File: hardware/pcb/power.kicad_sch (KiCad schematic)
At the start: 74 parts, among them J1 XT30PW-F, J12 Solar, J13 USB-C, Q3 AO3407, Q4 BSS123, Q5 AO3407, U1 AP63203WU, U11 USBLC6, U12 IP2326, U7 CN3722, U8 MT3608B

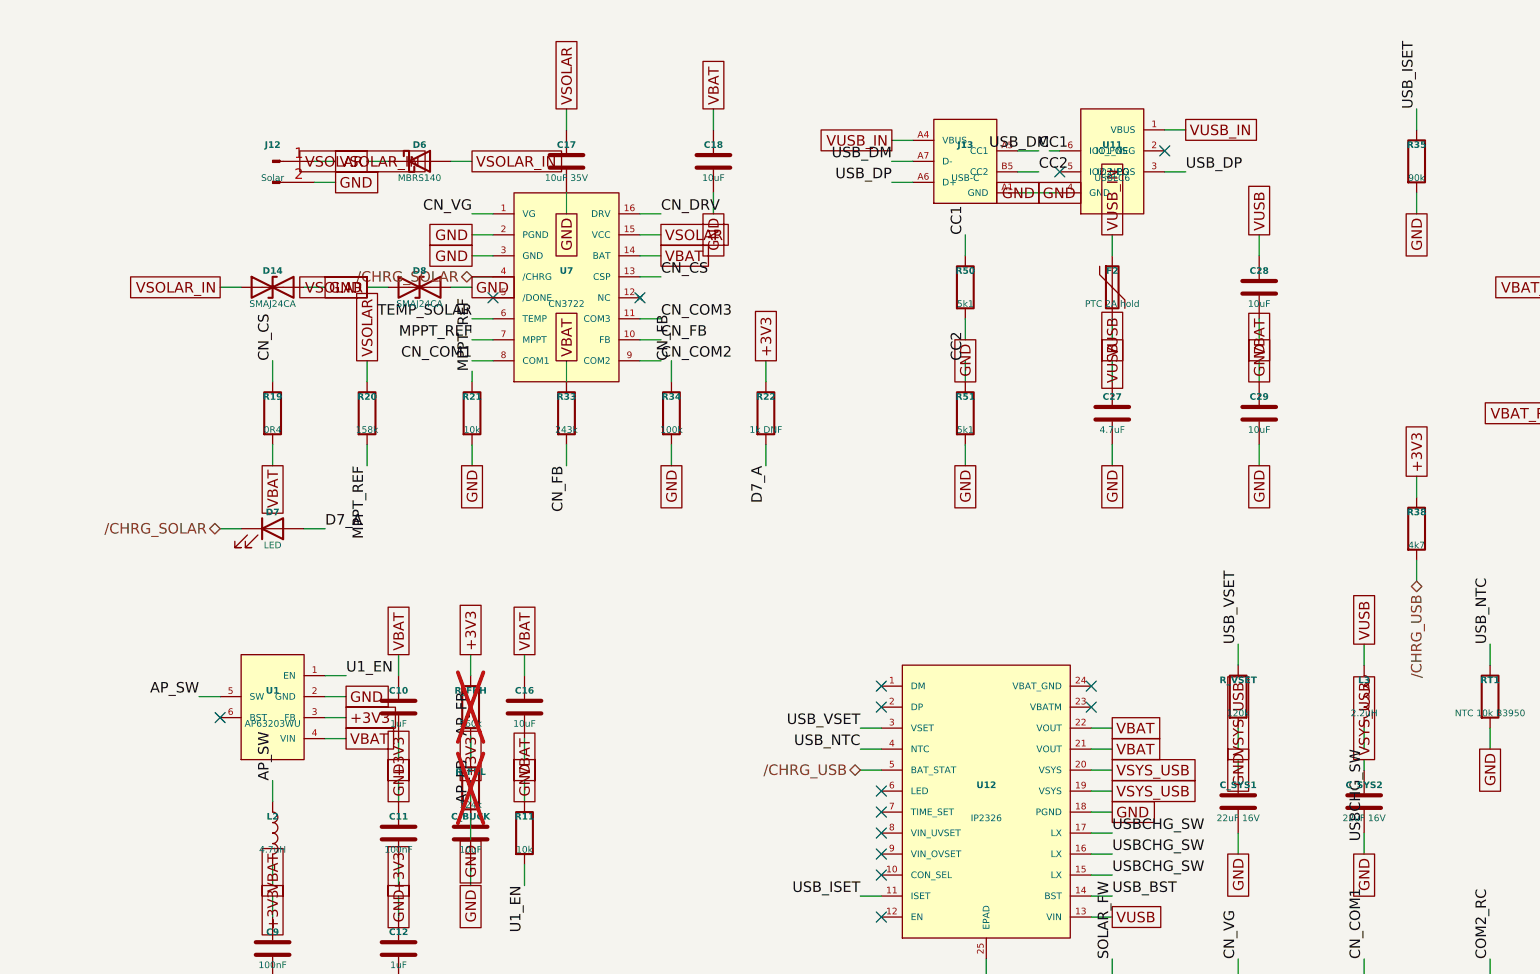
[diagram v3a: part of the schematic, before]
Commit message: hw(pcb): apply blocker #9 — AP63203 renumber + BST cap, ESD symbol fixes, value syncs
All eight required edits from the 2026-07-14 component verification,
applied by pin-name-preserving renumber (positions untouched, so the
stub+label wiring stays electrically identical; only footprint pad
mapping changes):

- U1: lib symbol renamed welld:AP63203WU, pins renumbered to the
  verified Diodes map (FB=1, EN=2, VIN=3, GND=4, SW=5, BST=6),
  footprint TSOT-23-6. NEW C_BST_AP 100 nF placed and wired on new net
  AP_BST (BST <-> SW) — the bootstrap cap without which the 3.3 V rail
  cannot start. BST no_connect removed.
- U11 USBLC6 renumbered to the ST map (I/O1=1, GND=2, I/O2=3, I/O2'=4,
  VBUS=5, I/O1'=6).
- D1/D12 PRTR5V0U2X redrawn as the real 4-pin SOT-143B (GND=1, I/O1=2,
  I/O2=3, VCC=4); phantom VCC2/GND2 pins, their 4 stubs and 4 labels
  removed; instance pin uuids pruned.
- D9/D10 -> SMAJ5.0A; U12 footprint -> QFN-24-1EP_4x4mm_P0.5mm;
  FB1 -> 0603; C28/C29/C_SYS1/C_SYS2 -> 25 V ratings.
- Intent tables in kicad_wire_script.py remapped placeholder-safe;
  netlist_check.py re-run: 393 pins, 78 nets (+AP_BST), 20 no-connects,
  ZERO mismatches. All five sheets pass the balance check.

Co-Authored-By: Claude Fable 5 <noreply@anthropic.com>
Claude-Session: https://claude.ai/code/session_01VtMFY5Q94iYbsNPpLcPJyK
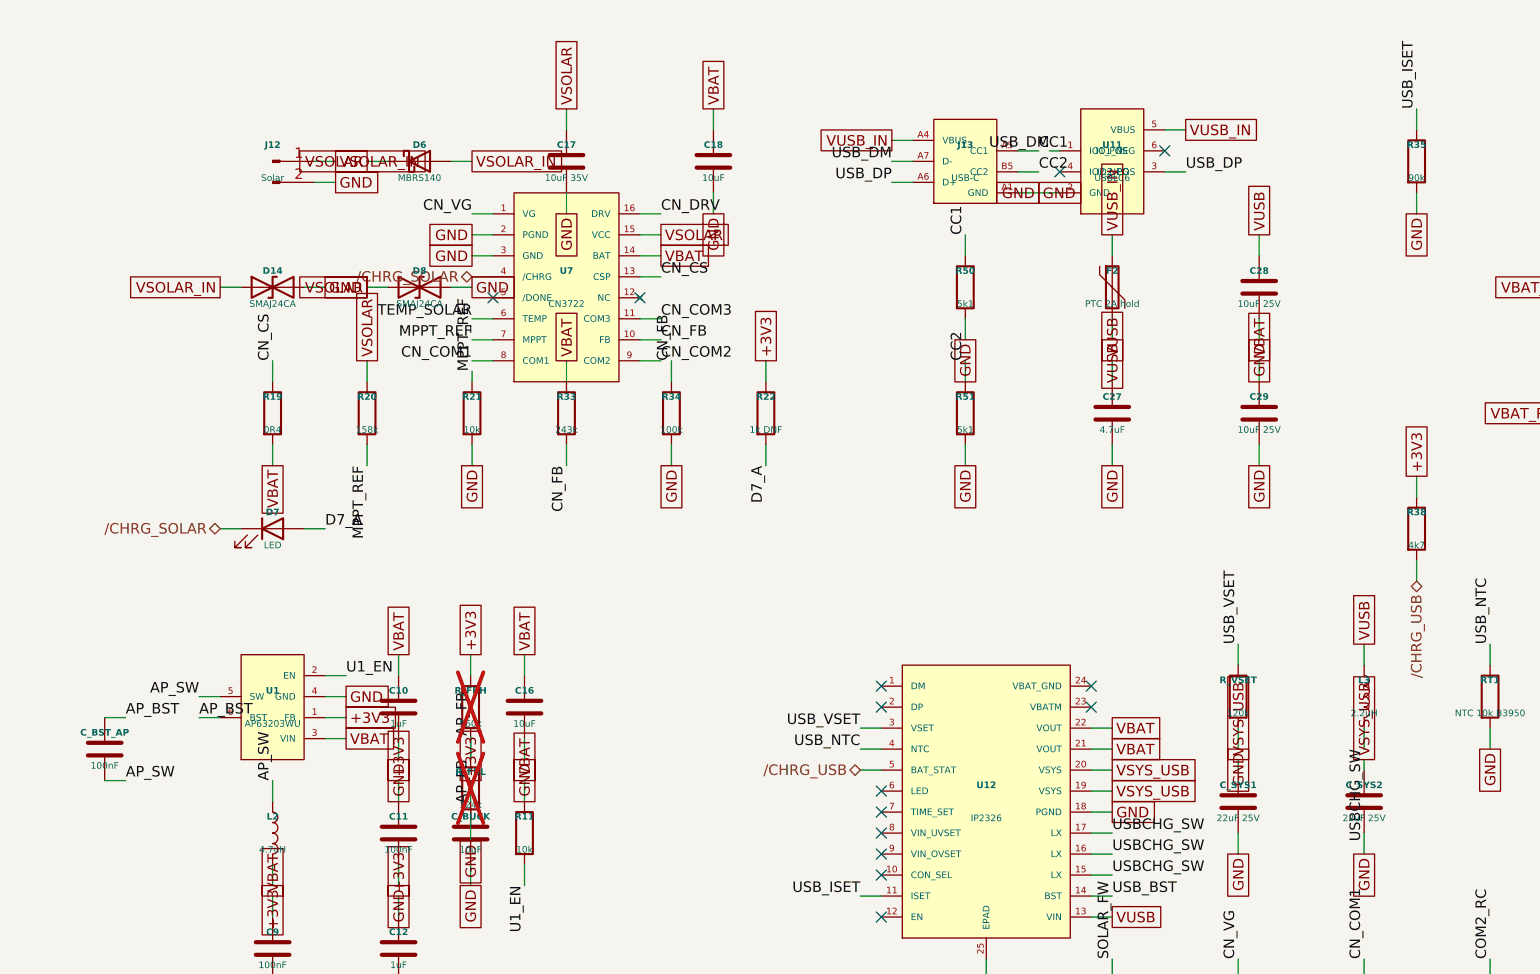
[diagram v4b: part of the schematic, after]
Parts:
- added C_BST_AP: 100nF, Capacitor_SMD:C_0402_1005Metric, symbol Device:C
- C28, C29: value 10uF -> 10uF 25V
- C_SYS1, C_SYS2: value 22uF 16V -> 22uF 25V
- U1: footprint Package_TO_SOT_SMD:SOT-23-6 -> Package_TO_SOT_SMD:TSOT-23-6; symbol welld:AP63205WU -> welld:AP63203WU
- U12: footprint welld:IP2326_TBD -> Package_DFN_QFN:QFN-24-1EP_4x4mm_P0.5mm_EP2.6x2.6mm
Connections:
- net +3V3: now also U1.1 (FB); no longer U1.3 (FB)
- net AP_SW: now also C_BST_AP.2
- net GND: now also U1.4 (GND), U11.2 (GND); no longer U1.2 (GND), U11.4 (GND)
- net U1_EN: now also U1.2 (EN); no longer U1.1 (EN)
- net USB_DM: now also U11.1 (IO1_POS); no longer U11.6 (IO1_POS)
- net VBAT: now also U1.3 (VIN); no longer U1.4 (VIN)
- net VUSB_IN: now also U11.5 (VBUS); no longer U11.1 (VBUS)
- net AP_BST: now reaches U1.6 (BST)
- net AP_BST: now also C_BST_AP.1
- no-connect marks 15 -> 14
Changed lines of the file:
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@@
 			)
 		)
-		(property "Value" "10uF"
+		(property "Value" "10uF 25V"
 			(at 185.42 41.37 0)
 			(show_name no)
@@
 	)
 	(symbol
-		(lib_id "welld:AP63205WU")
+		(lib_id "welld:AP63203WU")
 		(at 66.04 90.17 0)
 		(unit 1)
@@
 			)
 		)
-		(property "Footprint" "Package_TO_SOT_SMD:SOT-23-6"
+		(property "Footprint" "Package_TO_SOT_SMD:TSOT-23-6"
 			(at 0 0 0)
 			(hide yes)
@@
 			)
 		)
-		(property "Value" "10uF"
+		(property "Value" "10uF 25V"
 			(at 185.42 56.61 0)
 			(show_name no)
@@
 	(symbol
 		(lib_id "Device:C")
+		(at 45.72 95.25 0)
+		(unit 1)
+		(body_style 1)
+		(exclude_from_sim no)
+		(in_bom yes)
+		(on_board yes)
+		(in_pos_files yes)
+		(dnp no)
+		(fields_autoplaced yes)
+		(property "Reference" "C_BST_AP"
+			(at 45.72 93.25 0)
+			(show_name no)
+			(do_not_autoplace no)
+			(effects
+				(font
+					(size 0.8 0.8)
+					(bold yes)
+				)
+			)
+		)
+		(property "Value" "100nF"
+			(at 45.72 97.25 0)
+			(show_name no)
+			(do_not_autoplace no)
+			(effects
+				(font
+					(size 0.8 0.8)
+				)
+			)
+		)
+		(property "Footprint" "Capacitor_SMD:C_0402_1005Metric"
+			(at 0 0 0)
+			(hide yes)
+			(show_name no)
+			(do_not_autoplace no)
+			(effects
+				(font
+					(size 0.8 0.8)
+				)
+			)
+		)
+		(property "Datasheet" ""
+			(at 0 0 0)
+			(hide yes)
+			(show_name no)
+			(do_not_autoplace no)
+			(effects
+				(font
+					(size 0.8 0.8)
+				)
+			)
+		)
+		(property "Description" "100nF 0402 MT3608B bootstrap cap BST(pin6)->SW mandatory gate driver supply"
+			(at 0 0 0)
+			(hide yes)
+			(show_name no)
+			(do_not_autoplace no)
+			(effects
+				(font
+					(size 0.8 0.8)
+				)
+			)
+		)
+		(property "LCSC" "C14663"
+			(at 0 0 0)
+			(hide yes)
+			(show_name no)
+			(do_not_autoplace no)
+			(effects
+				(font
+					(size 0.8 0.8)
+				)
+			)
+		)
+		(pin "1"
+		)
+		(pin "2"
+		)
+		(instances
+			(project "welld"
+				(path "/58c9365f-ec30-52a7-98fc-0e15b15bee29"
+					(reference "C_BST_AP")
+					(unit 1)
+				)
+				(path "/58c9365f-ec30-52a7-98fc-0e15b15bee29/64fba67a-e021-5c3c-b6fb-14c5c55ee35f/aaaa0003-b000-4000-8000-000000000001"
+					(reference "C_BST_AP")
+					(unit 1)
+				)
+			)
+		)
+	)
+	(symbol
+		(lib_id "Device:C")
 		(at 90 105.41 0)
 		(unit 1)
@@
 			)
 		)
-		(property "Footprint" "welld:IP2326_TBD"
+		(property "Footprint" "Package_DFN_QFN:QFN-24-1EP_4x4mm_P0.5mm_EP2.6x2.6mm"
 			(at 0 0 0)
 			(hide yes)
@@
 			)
 		)
-		(property "Value" "22uF 16V"
+		(property "Value" "22uF 25V"
 			(at 182.88 103.6 0)
 			(show_name no)
@@
 			)
 		)
-		(property "Value" "22uF 16V"
+		(property "Value" "22uF 25V"
 			(at 198.12 103.6 0)
 			(show_name no)
@@
 	(wire
 		(pts
+			(xy 57.15 91.44) (xy 59.69 91.44)
+		)
+		(stroke
+			(width 0)
+			(type default)
+		)
+	)
+	(label "AP_BST"
+		(at 57.15 91.44 0)
+		(effects
+			(font
+				(size 1.27 1.27)
+			)
+			(justify left bottom)
+		)
+	)
+	(wire
+		(pts
+			(xy 45.72 91.44) (xy 48.26 91.44)
+		)
+		(stroke
+			(width 0)
+			(type default)
+		)
+	)
+	(label "AP_BST"
+		(at 48.26 91.44 0)
+		(effects
+			(font
+				(size 1.27 1.27)
+			)
+			(justify left bottom)
+		)
+	)
+	(wire
+		(pts
+			(xy 45.72 99.06) (xy 48.26 99.06)
+		)
+		(stroke
+			(width 0)
+			(type default)
+		)
+	)
+	(label "AP_SW"
+		(at 48.26 99.06 0)
+		(effects
+			(font
+				(size 1.27 1.27)
+			)
+			(justify left bottom)
+		)
+	)
+	(wire
+		(pts
 			(xy 72.39 91.44) (xy 74.93 91.44)
 		)
@@
 	)
 	(no_connect
-		(at 59.69 91.44)
-	)
-	(no_connect
